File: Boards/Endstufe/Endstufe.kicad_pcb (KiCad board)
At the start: 2 copper layers, 153 x 110 mm, 56 parts, among them J1 HV In, J2 Relais, J3 NF_In, K1 G6E, P2 Trafo, P4 6V3_AC, P5 Trafo_GK, P6 6V3_DC, P7 VSup1, P8 Bias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

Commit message: Layout changes after migrate to Kicad 5.1
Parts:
- removed P2: Trafo, TerminalBlock_RND:TerminalBlock_RND_205-00004_1x05_P5.00mm_Horizontal
- added J4: Conn_01x06, Connector_TE-Connectivity:TE_MATE-N-LOK_1-770875-x_2x03_P4.14mm_Vertical, F.Cu at (201.8, 106.8)
- J3: footprint Connector_Molex:Molex_KK-254_AE-6410-02A_1x02_P2.54mm_Vertical -> Connector_JST:JST_EH_B2B-EH-A_1x02_P2.50mm_Vertical
- moved RV2 14.6 mm to (65.9, 77.0), turned to 90 degrees
- moved J2 12.8 mm to (65.3, 138.6)
- moved P7 8.02 mm to (191.0, 114.4), turned to 180 degrees
- moved C7 5.46 mm to (71.6, 108.1)
- moved J3 3.14 mm to (65.3, 111.9), turned to 90 degrees
- moved R9 2.79 mm to (71.6, 117.0), turned to 0 degrees
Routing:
- net Net-(R3-Pad1): track 5.08 -> 19.8 mm
- net +240V: track 26.0 -> 14.0 mm
- net Net-(D1-Pad1): track 12.1 -> 23.4 mm
- net Net-(J4-Pad5): track 46.1 -> 55.5 mm
- net Net-(J4-Pad1): track 32.6 -> 41.3 mm
- net Net-(C7-Pad2): track 27.1 -> 32.7 mm
- net Net-(R18-Pad2): track 4.85 -> 9.79 mm
- net Net-(D1-Pad2): track 12.5 -> 16.0 mm
- net -120V: track 55.7 -> 52.3 mm
- net Net-(J4-Pad6): track 13.5 -> 10.5 mm
- net Net-(J4-Pad4): track 18.6 -> 21.2 mm
- net Net-(C7-Pad1): track 29.8 -> 27.2 mm
- net +300V: track 99.7 -> 100.8 mm
- net Net-(C10-Pad2): track 41.9 -> 42.6 mm
- net +450V: track 10.4 -> 11.1 mm

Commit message: Minor Layout changes
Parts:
- moved RV2 13.8 mm to (76.2, 86.2), turned to 180 degrees
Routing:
- net Net-(R3-Pad1): track 19.8 -> 6.22 mm
- net +240V: track 14.0 -> 24.9 mm
- net Net-(R18-Pad2): track 9.79 -> 4.38 mm
- net Net-(C7-Pad2): track 32.7 -> 30.8 mm
- net Net-(P6-Pad1): track 42.9 -> 41.5 mm

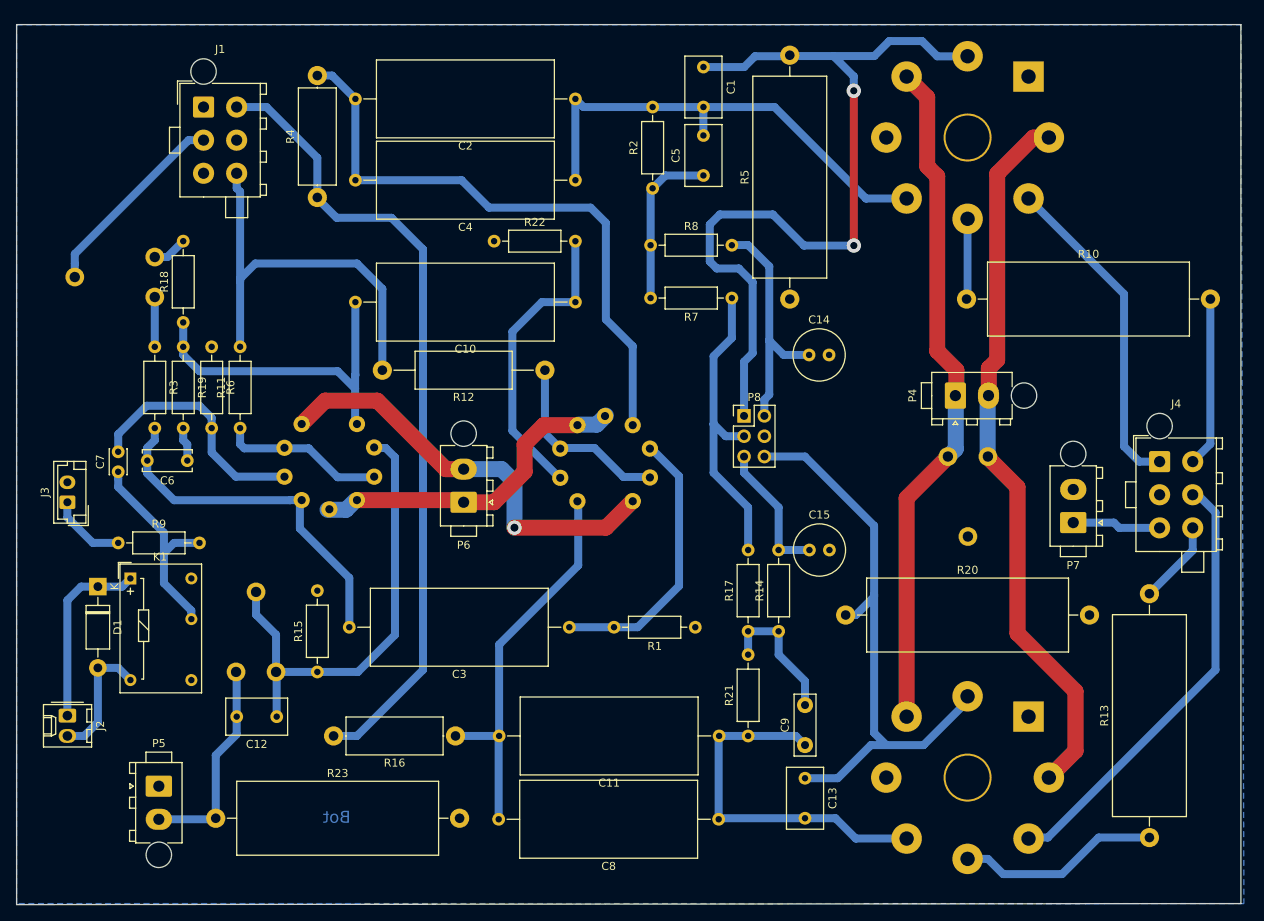
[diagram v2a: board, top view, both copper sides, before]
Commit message: Layout changes, Supply connector changes, Mounting holes
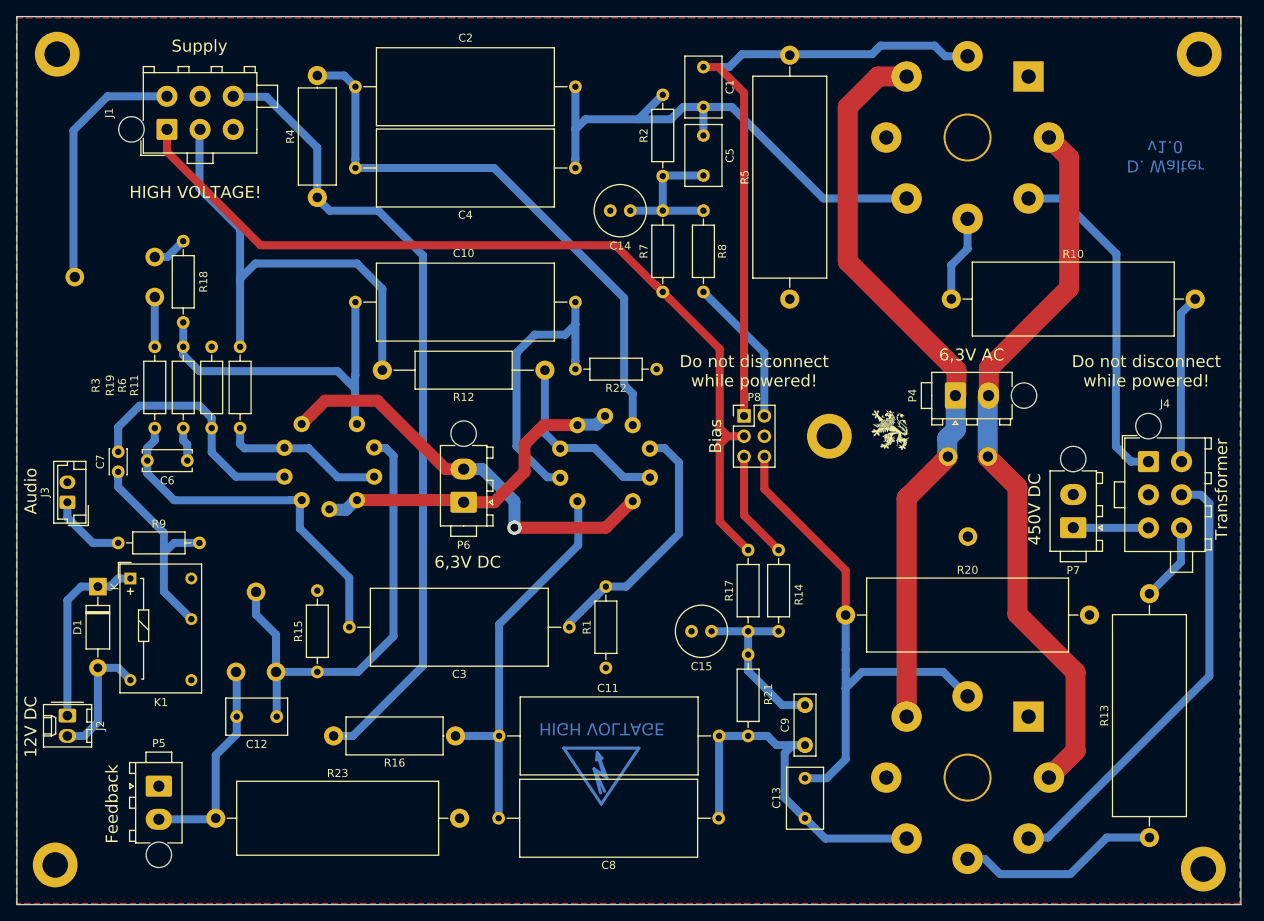
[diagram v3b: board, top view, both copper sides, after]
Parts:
- added G***: LOGO, Loewe:Loewe_Klein, B.Cu at (202.2, 76.7)
- added G***: LOGO, Loewe:Loewe_Klein, F.Cu at (168.1, 102.9)
- added REF**: MountingHole_3.2mm_M3_DIN965_Pad, MountingHole:MountingHole_3.2mm_M3_DIN965_Pad, F.Cu at (64.0, 55.9)
- added REF**: MountingHole_3.2mm_M3_DIN965_Pad, MountingHole:MountingHole_3.2mm_M3_DIN965_Pad, F.Cu at (63.8, 157.2)
- added REF**: MountingHole_3.2mm_M3_DIN965_Pad, MountingHole:MountingHole_3.2mm_M3_DIN965_Pad, F.Cu at (207.3, 157.7)
- added REF**: MountingHole_3.2mm_M3_DIN965_Pad, MountingHole:MountingHole_3.2mm_M3_DIN965_Pad, F.Cu at (206.8, 55.9)
- added REF**: MountingHole_3.2mm_M3_DIN965_Pad, MountingHole:MountingHole_3.2mm_M3_DIN965_Pad, F.Cu at (160.5, 103.6)
- added REF**: Symbol_HighVoltage_Type2_CopperTop_VerySmall, Symbol:Symbol_HighVoltage_Type2_CopperTop_VerySmall, B.Cu at (132.0, 145.4)
- J4: value Conn_01x06 -> Trafo
- moved C14 28.7 mm to (135.6, 75.4), turned to 180 degrees
- moved R22 25.9 mm to (138.9, 95.2), turned to 180 degrees
- moved C15 15.9 mm to (145.8, 128.0), turned to 180 degrees
- moved R1 12.3 mm to (132.6, 132.6), turned to 90 degrees
- moved R7 8.67 mm to (139.7, 85.6), turned to 90 degrees
- moved R8 7.89 mm to (144.8, 75.4), turned to 270 degrees
- moved J1 5.36 mm to (77.7, 65.3), turned to 90 degrees
- moved R2 1.98 mm to (139.7, 71.1)
- moved R10 1.91 mm to (175.8, 86.5)
- moved C2 1.52 mm to (128.8, 59.9)
- moved C4 1.52 mm to (128.8, 70.1)
- moved J4 1.40 mm to (200.4, 106.8)
- moved P7 0.63 mm to (191.0, 115.1)
- moved C8 0.13 mm to (146.7, 151.4)
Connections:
- C5 pad 1: UG_1 -> Net-(C14-Pad1)
- C9 pad 2: UG_2 -> Net-(C15-Pad1)
- J1 pad 1: GND -> -60V
- J1 pad 2: +240V -> -120V
- J1 pad 4: +300V -> +240V
- J1 pad 6: -120V -> +300V
- K1 pad 12: (no net) -> Net-(K1-Pad12)
- P8 pad 2: Net-(C14-Pad1) -> UG_1
- P8 pad 5: Net-(C15-Pad1) -> UG_2
- R14 pad 1: UG_2 -> Net-(C15-Pad1)
- R14 pad 2: Net-(C15-Pad1) -> UG_2
- R17 pad 1: UG_2 -> Net-(C15-Pad1)
- R2 pad 1: UG_1 -> Net-(C14-Pad1)
- R21 pad 2: UG_2 -> Net-(C15-Pad1)
- R7 pad 2: UG_1 -> Net-(C14-Pad1)
- R8 pad 1: UG_1 -> Net-(C14-Pad1)
- R8 pad 2: Net-(C14-Pad1) -> UG_1
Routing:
- net -60V: track 38.7 -> 111.6 mm
- net Bias_1: track 108.4 -> 81.6 mm, vias 2 -> 0
- net Net-(C14-Pad1): track 30.5 -> 18.6 mm
- net Bias_2: track 75.0 -> 65.5 mm
- net Net-(P4-Pad1): track 85.2 -> 93.4 mm
- net -120V: track 52.3 -> 59.4 mm
- net +240V: track 24.9 -> 31.8 mm
- net Net-(C1-Pad2): track 60.3 -> 65.3 mm
- net Net-(C15-Pad1): track 17.3 -> 22.2 mm
- net Net-(C2-Pad2): track 76.4 -> 72.2 mm
- net UG_2: track 17.3 -> 13.5 mm
- net Net-(C3-Pad1): track 34.6 -> 32.0 mm
- net UG_1: track 20.8 -> 18.7 mm
- net Net-(C10-Pad1): track 37.9 -> 36.1 mm
- net +450V: track 11.1 -> 9.41 mm
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- added copper zone on F.Cu, net GND
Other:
- board size 153 x 110 mm -> 153 x 111 mm
- board text added: "12V DC"
- board text added: "450V DC"
- board text added: "6,3V AC"
- board text added: "6,3V DC"
- board text added: "Audio"
- board text added: "Bias"
- board text added: "D. Walter v1.0"
- board text added: "Do not disconnect while powered!"
- board text added: "Driver Bias Adjust"
- board text added: "Feedb. Adjust"
- board text added: "Feedback"
- board text added: "HIGH VOLTAGE"
- board text added: "HIGH VOLTAGE!"
- board text added: "Heater Adjust"
- board text added: "Supply"
- board text added: "Transformer"
- board text removed: "Bot"

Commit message: Added Vias & Mounting Holes
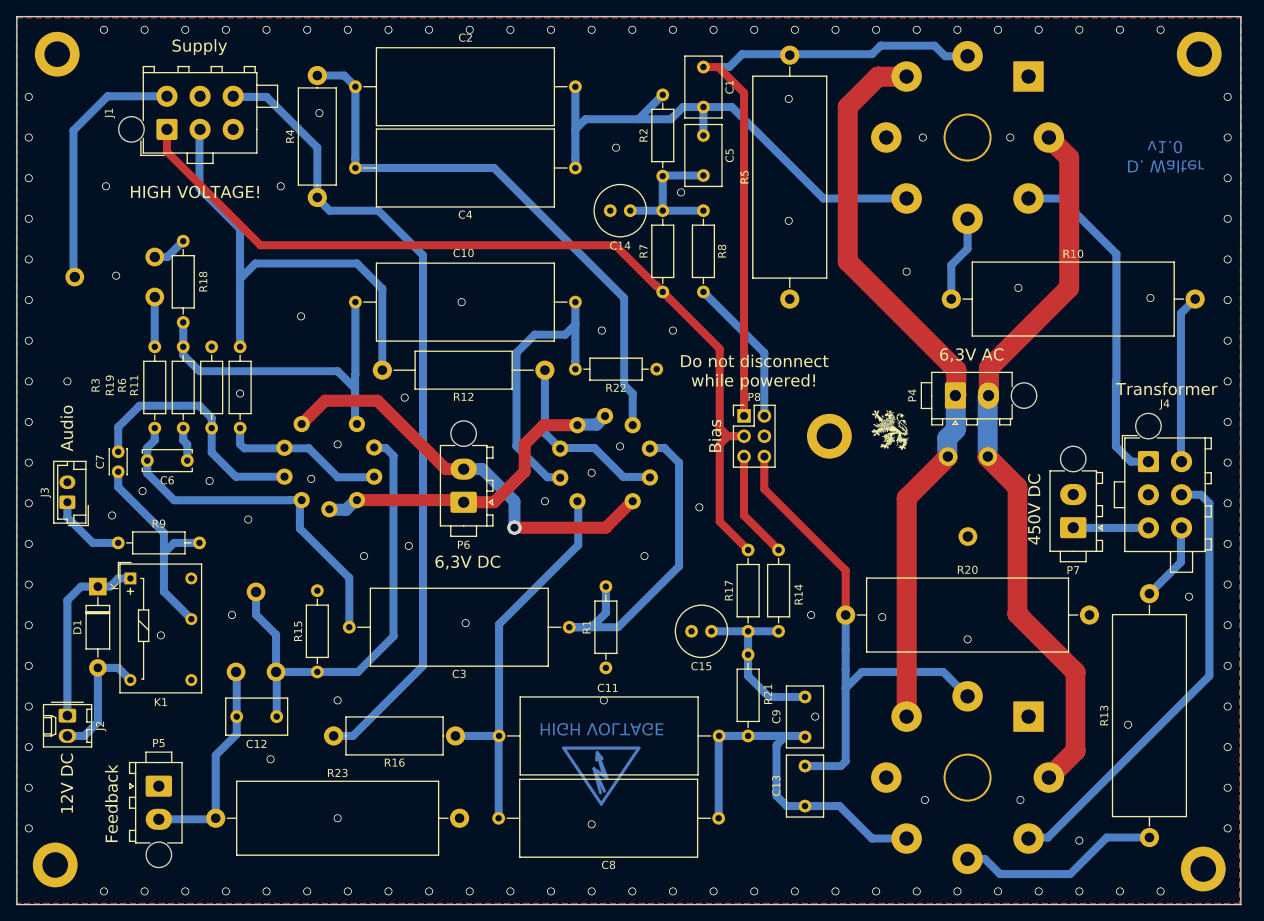
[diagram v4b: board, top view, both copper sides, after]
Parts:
- C9: footprint Capacitor_THT:C_Disc_D7.5mm_W2.5mm_P5.00mm -> Capacitor_THT:C_Disc_D7.5mm_W4.4mm_P5.00mm
- moved C13 1.52 mm to (157.5, 144.9)
- moved C9 1.02 mm to (157.5, 141.2)
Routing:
- net Net-(C3-Pad1): track 32.0 -> 41.5 mm
- net GND: vias 0 -> 142
